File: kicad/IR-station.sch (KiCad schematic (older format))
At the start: 34 parts, among them P1 I2C, P2 ADC, P3 GPIO, P4 USB_Power, Q1 IRLML6344, SW1 BUTTON, U1 ESP-WROOM-02-2, U2 OSRB38C9AA, U3 NJU7223, U4 AE-FT234X

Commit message: 部品表を更新
黄色プリント基板バージョン
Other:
- note added: "IR-Station ver. 2016-09-22"
- note removed: "IR-Station ver. 2016-08-25"
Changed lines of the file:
@@
 	1550 3950 4950 3950
 Text Notes 1600 1300 0    100  ~ 0
-IR-Station ver. 2016-08-25
+IR-Station ver. 2016-09-22
 $Comp
 L AE-FT234X U4

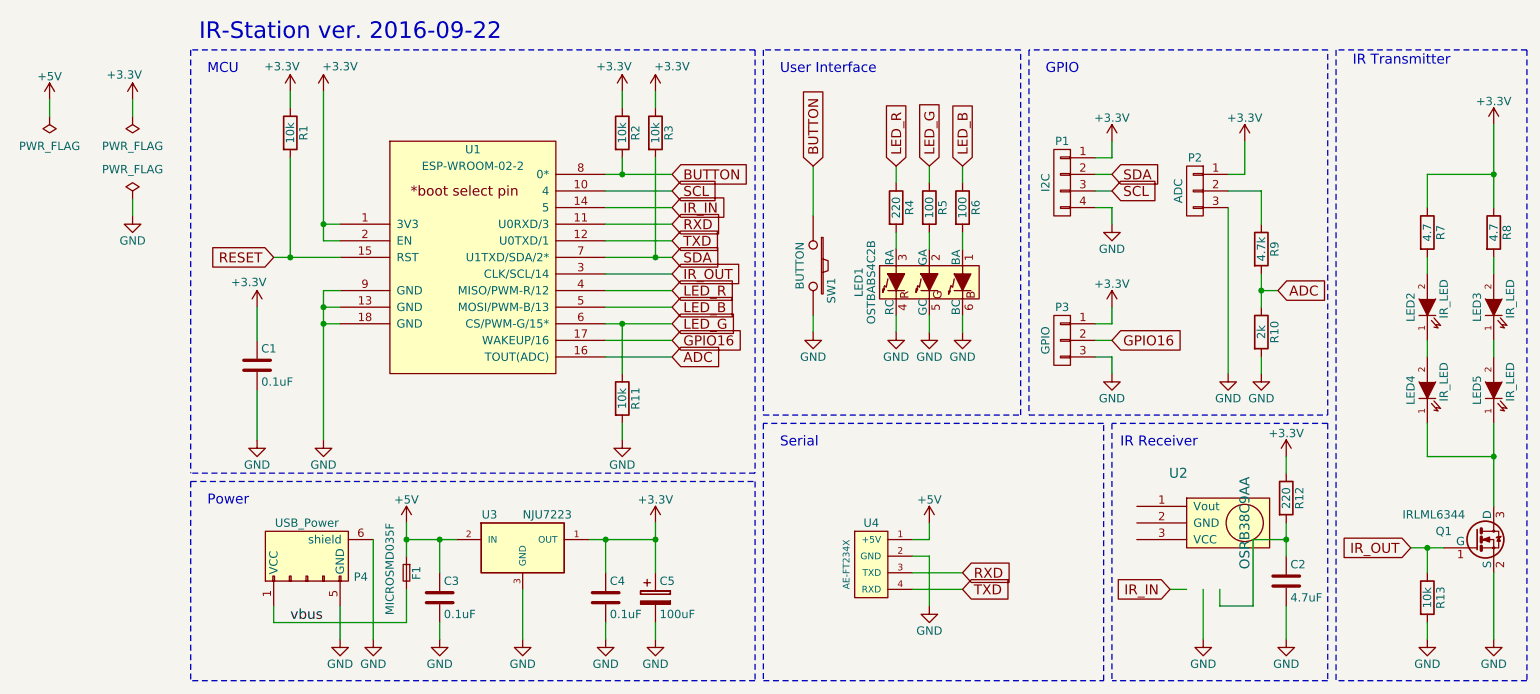
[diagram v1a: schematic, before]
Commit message: 新しく基板を作成
レギュレータを小型のものに変更
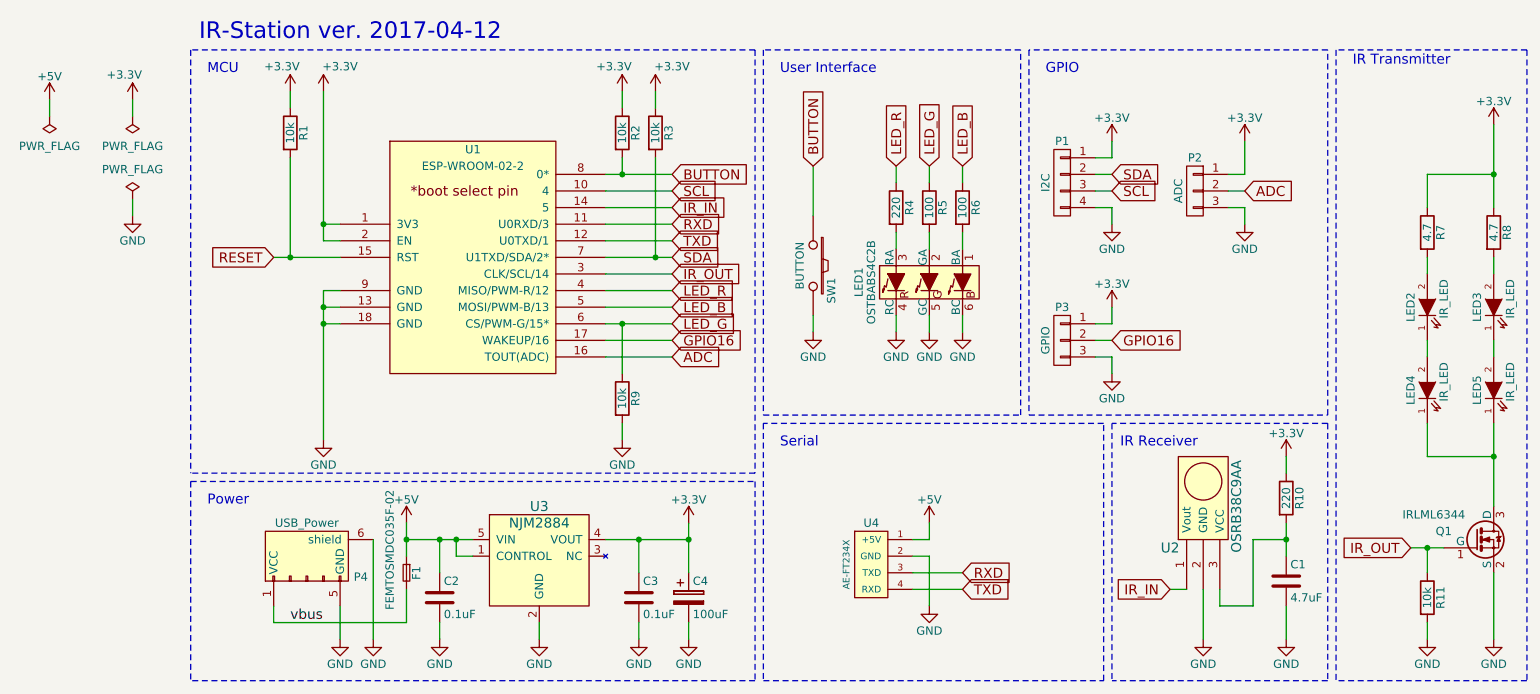
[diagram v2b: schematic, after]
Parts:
- removed C1: 0.1uF, Capacitors_SMD:C_0603, symbol C
- removed R10: 2k, Resistors_SMD:R_0603, symbol R
- removed R9: 4.7k, Resistors_SMD:R_0603, symbol R
- removed U3: NJU7223, TO_SOT_Packages_SMD:TO-252-2Lead, symbol NJU7223
- added U3: NJM2884, TO_SOT_Packages_SMD:SOT89-5_Housing, symbol NJM2884
- F1: value MICROSMD035F -> FEMTOSMDC035F-02; footprint SMD_Packages:SMD-1210_Pol -> Resistors_SMD:R_0603
- LED1: footprint kerikun11:OSTBABS4C2B -> IR-station:OSTBABS4C2B
- P4: footprint kerikun11:USB_Micro_B_Power -> IR-station:USB_Micro_B_Power
- SW1: footprint kerikun11:SW_PUSH -> IR-station:SW_PUSH
- U1: footprint kerikun11:ESP-WROOM-02 -> IR-station:ESP-WROOM-02
- U2: footprint kerikun11:PL-IRMxxxx_Angle -> IR-station:PL-IRMxxxx_Angle
- U4: footprint Connectors_JST:JST_GH_BM04B-GHS-TBT_04x1.25mm_Straight -> Pin_Headers:Pin_Header_Straight_1x04
- renumbered C2 to C1, C3 to C2, C4 to C3, C5 to C4, R12 to R10, R13 to R11, R11 to R9
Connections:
- net +3V3: now also U3.4 (VOUT)
- net +5V: now also U3.1 (CONTROL), U3.5 (VIN)
- net ADC: now also P2.2 (P2)
- net GND: now also U2.2 (GND), U3.2 (GND)
- net IR_IN: now also U2.1 (Vout)
- net at U2.3 (VCC): now also C1.1, R10.2
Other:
- note added: "IR-Station ver. 2017-04-12"
- note removed: "IR-Station ver. 2016-09-22"
- moved on the sheet: C3, C4, U2

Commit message: 新基板用に部品表や画像を更新
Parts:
- LED2, LED3, LED4, LED5: symbol LED -> LED-RESCUE-IR-station
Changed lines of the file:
@@
 EESchema Schematic File Version 2
+LIBS:IR-station-rescue
 LIBS:power
 LIBS:device
@@
 $EndComp
 $Comp
-L LED LED2
+L LED-RESCUE-IR-station LED2
 U 1 1 57669630
 P 9000 2900
@@
 $EndComp
 $Comp
-L LED LED4
+L LED-RESCUE-IR-station LED4
 U 1 1 5766A81B
 P 9000 3400
@@
 $EndComp
 $Comp
-L LED LED5
+L LED-RESCUE-IR-station LED5
 U 1 1 5766A87E
 P 9400 3400
@@
 $EndComp
 $Comp
-L LED LED3
+L LED-RESCUE-IR-station LED3
 U 1 1 5766A8D8
 P 9400 2900
